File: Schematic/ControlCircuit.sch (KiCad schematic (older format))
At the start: 26 parts, among them J201 JACK-PWR, Q201 2N2222, Q202 2N2222, U201 ICM7555, U202 ARDUINO_Pro-Mini, U203 74HC595, U204 74HC595, U205 74HC165, U206 74HC165

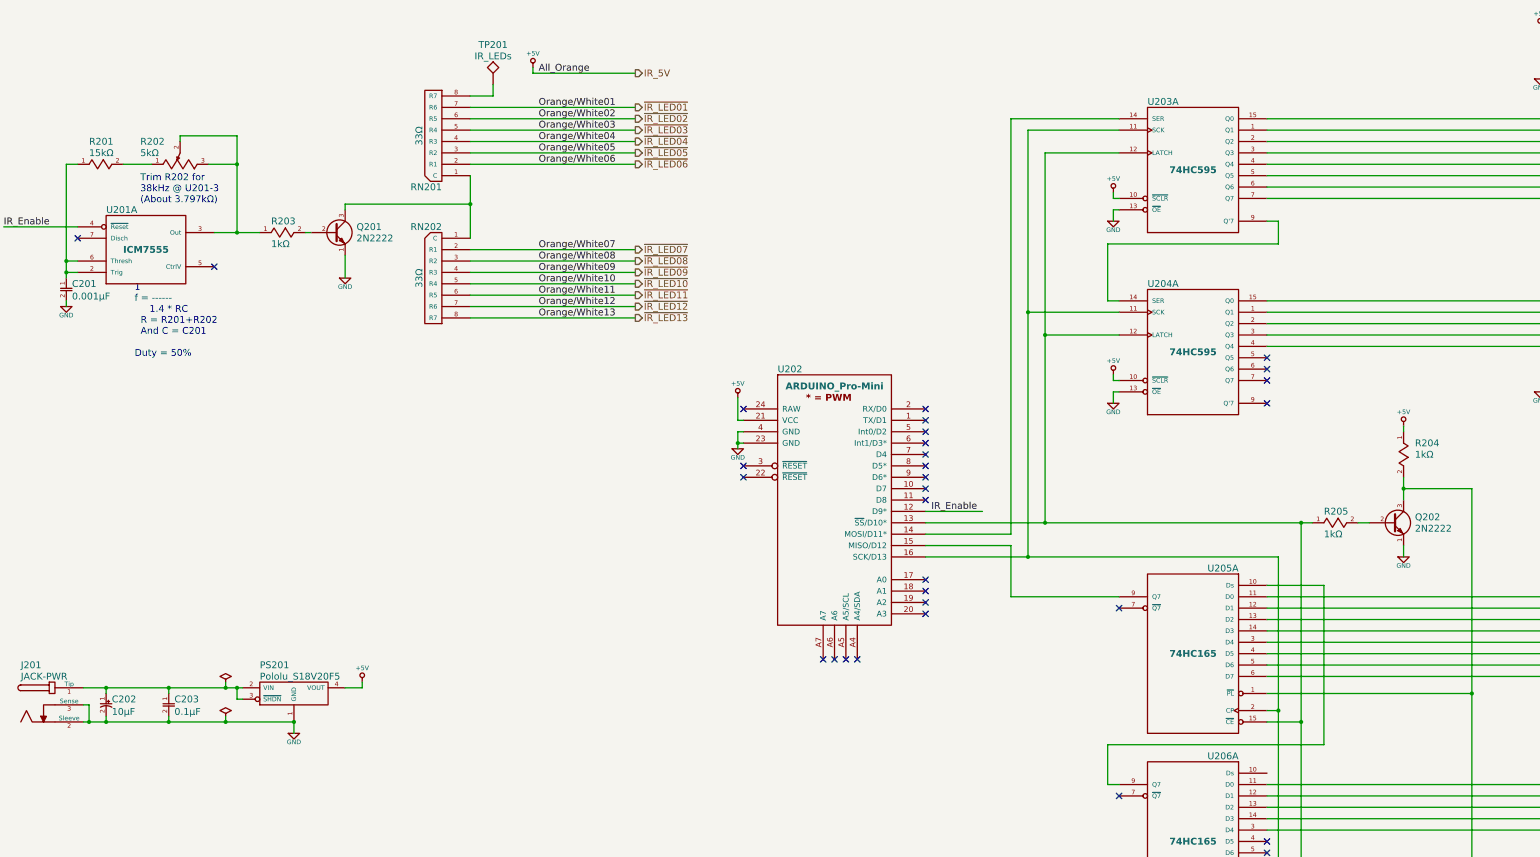
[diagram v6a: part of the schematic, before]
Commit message: Schematic v1.2.4 - Change all 2N2222 BJT to VN3205 N-MOSFET (and remove base/gate resistors.) CyclingRainbow.ino v0.1.1 - Incorporate code from CyclingLEDTimingTest.ino and remove single-switch logic. Ready for first load into prototype hardware.
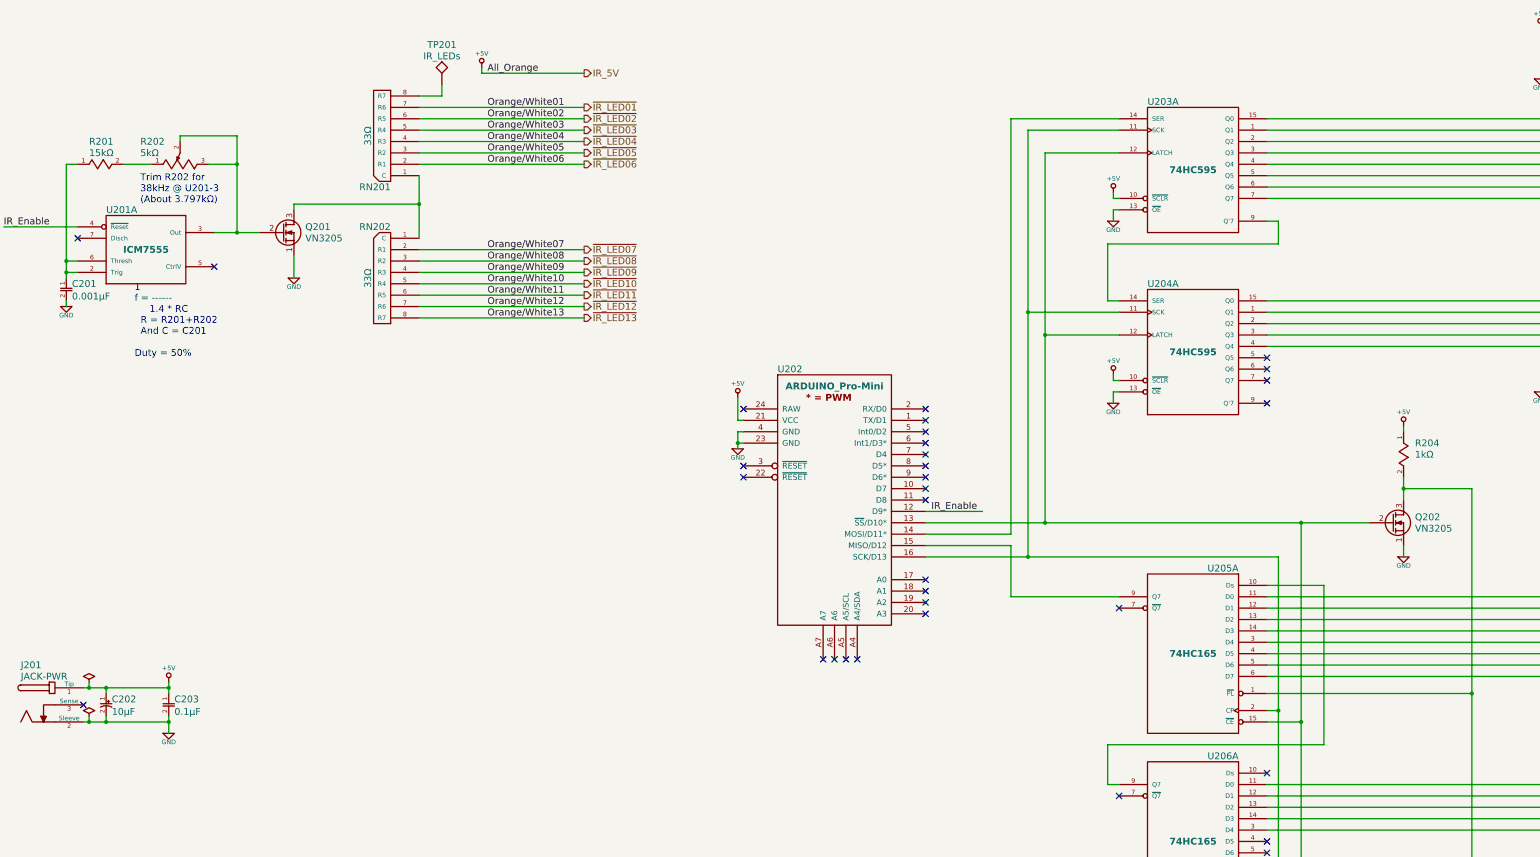
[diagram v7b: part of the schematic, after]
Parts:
- removed PS201: Pololu_S18V20F5, symbol Pololu_S18V20F5
- removed Q201, Q202: 2N2222, symbol Q_NPN_EBC
- removed R203, R205: 1kΩ, symbol RES
- added Q201, Q202: VN3205, TO_SOT_Packages_THT:TO-92_Inline_Wide, symbol Q_NMOS_SGD
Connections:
- net +5V: now also C202.1, C203.1, J201.1 (Tip)
- net GND: now also Q201.1 (S), Q202.1 (S); no longer J201.3 (Sense)
- net at U202.13 (~SS~/D10*), U203.12 (LATCH), U204.12 (LATCH)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: now also Q202.2 (G)
- net at R202.2 (Wiper), R202.3, U201.3 (Out): now also Q201.2 (G)
- net at RN201.1 (C), RN202.1 (C): now also Q201.3 (D)
- net at R204.2, U205.1 (~PL), U206.1 (~PL): now also Q202.3 (D)
- no-connect marks 31 -> 33
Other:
- moved on the sheet: RN201, RN202, TP201
